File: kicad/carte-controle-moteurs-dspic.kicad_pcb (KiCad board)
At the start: 4 copper layers, 137.2 x 81.3 mm, 73 parts, among them J1 PDB, J10 PWR_IN, J11 GND, J12 5V, J13 3.3V, J14 EN, J15 MOTEUR 1, J16 MOTEUR 2, J17 L1, J18 H1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

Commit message: Optimisation de l'emplacement des composants et de la sérigraphie
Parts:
- ?: renamed from REF**; value Heatsink_Stonecold_HS-132_32x14mm_2xFixation1.5mm -> (none)
- moved R1 16.5 mm to (62.2, 77.5)
- moved R2 13.3 mm to (59.1, 59.7)
- moved U1 10.8 mm to (54.0, 77.5)
- moved ? 10.8 mm to (39.4, 68.6)
- moved J3 9.53 mm to (102.2, 43.2)
- moved C4 8.91 mm to (61.0, 66.7)
- moved C5 8.91 mm to (69.8, 69.2)
- moved RR1 6.38 mm to (129.5, 52.7)
- moved R10 5.08 mm to (129.5, 102.9)
- moved R11 5.08 mm to (124.5, 102.9)
- moved R5 5.08 mm to (108.0, 102.9)
- moved R6 5.08 mm to (105.4, 102.9)
- moved R7 5.08 mm to (100.3, 102.9)
- moved R8 5.08 mm to (132.1, 102.9)
- moved J16 2.84 mm to (118.1, 102.9)
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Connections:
- J10 pad 4: Net-(J10-Pad4) -> (no net)
- J3 pad 1: Net-(J3-Pad1) -> (no net)
- J3 pad 3: Net-(J3-Pad3) -> (no net)
- J6 pad 1: Net-(J6-Pad1) -> (no net)
- J7 pad 1: Net-(J7-Pad1) -> (no net)
- J8 pad 1: Net-(J8-Pad1) -> (no net)
- J9 pad 1: Net-(J9-Pad1) -> (no net)
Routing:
- net Net-(D10-Pad1): track 150.6 -> 137.0 mm
- net /ENABLE: track 91.1 -> 78.0 mm
- net /ALIM_PILES: track 122.5 -> 110.2 mm
- net /QEI1_CHA: track 89.1 -> 77.7 mm
- net /PWM1_H2: track 81.1 -> 70.2 mm
- net /DEBUG_TX: track 40.0 -> 29.3 mm
- net /DEBUG_RX: track 40.8 -> 30.1 mm
- net Net-(D11-Pad1): track 118.5 -> 127.6 mm
- net /PDB: track 58.6 -> 51.3 mm
- net /PWM1_L2: track 83.2 -> 76.2 mm
- net /QEI2_CHA: track 76.6 -> 70.2 mm
- net /QEI1_INDEX: track 88.2 -> 82.1 mm
- net Net-(R1-Pad1): track 2.54 -> 8.25 mm
- net /Mclr: track 58.3 -> 52.8 mm
- net /I2C_DATA: track 98.9 -> 104.2 mm
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
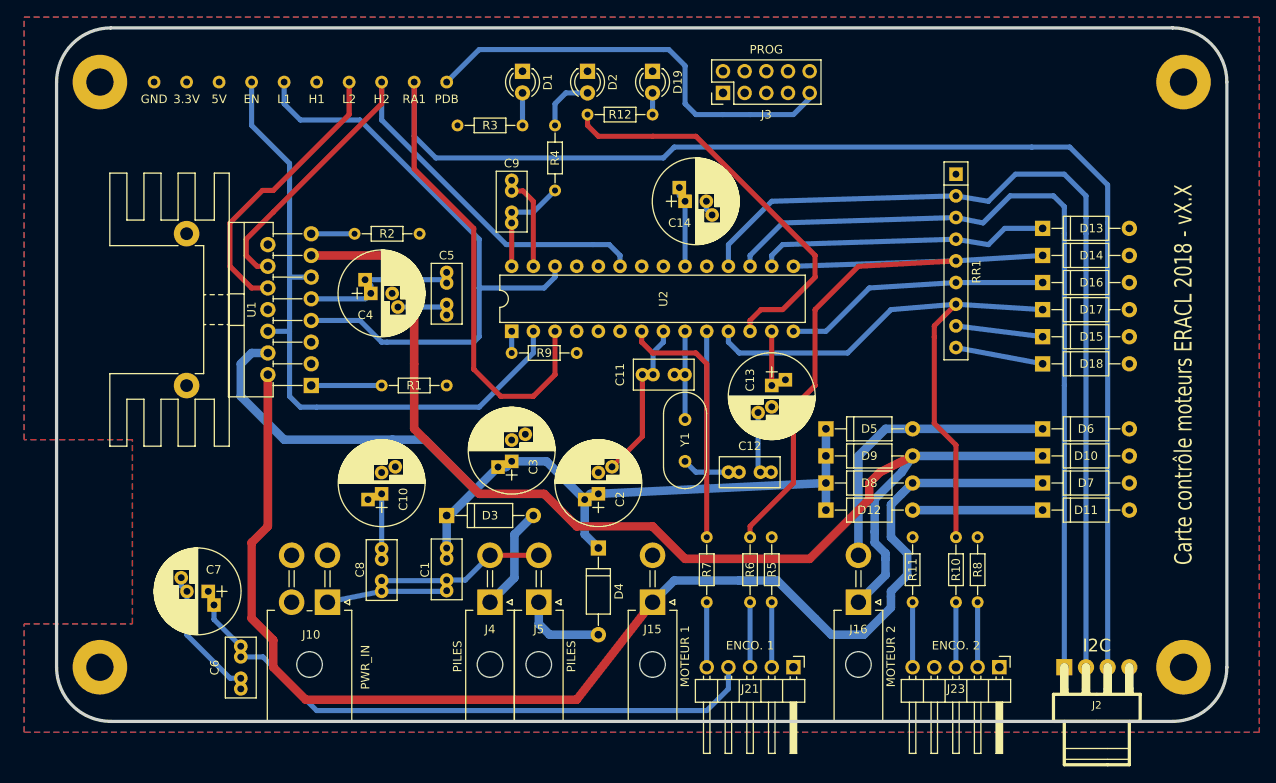
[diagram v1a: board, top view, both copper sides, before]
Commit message: Optimisation du tracé des pistes et des plans et validation typon
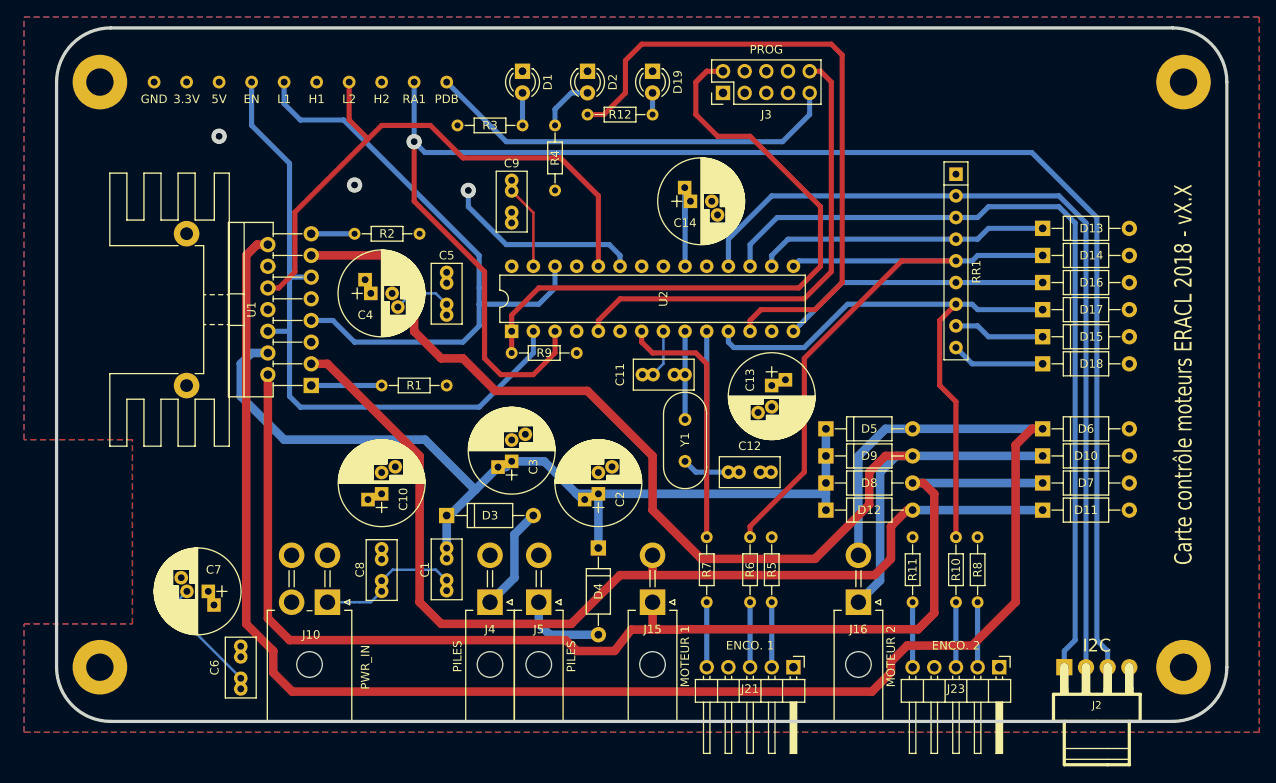
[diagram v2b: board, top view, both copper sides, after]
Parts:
- moved C14 0.63 mm to (98.4, 55.9)
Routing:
- net +5V: track 69.5 -> 201.5 mm, vias 0 -> 1
- net Net-(D5-Pad2): track 137.7 -> 203.2 mm
- net GND: track 98.8 -> 61.2 mm
- net Net-(R12-Pad2): track 47.8 -> 76.6 mm
- net /Mclr: track 52.8 -> 78.4 mm
- net +3V3: track 46.9 -> 28.1 mm
- net /RA1: track 201.1 -> 185.4 mm, vias 0 -> 1
- net Net-(D11-Pad1): track 127.6 -> 118.7 mm
- net Net-(D7-Pad1): track 153.2 -> 145.8 mm
- net /PWM1_L2: track 76.2 -> 70.0 mm
- net /QEI2_CHB: track 81.8 -> 76.9 mm
- net /PWM1_H1: track 70.9 -> 75.7 mm, vias 0 -> 1
- net /PWM1_H2: track 70.2 -> 66.5 mm, vias 0 -> 1
- net /I2C_DATA: track 104.2 -> 100.6 mm
- net /PDT: track 68.1 -> 64.8 mm
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- added copper zone on Interne3, net +3V3
- removed copper zone on Interne2, net +3V3
- removed copper zone on Interne3, net +5V
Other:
- net class planes added: clearance 0.254, trace_width 0.3, via_dia 1.80086, via_drill 0.8001

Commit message: Mise à jour de la version dans les cartouches et la sérigraphie
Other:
- board text added: "Carte contrôle moteurs ERACL 2018 - v1.0"
- board text removed: "Carte contrôle moteurs ERACL 2018 - vX.X"
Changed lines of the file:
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@@
     (links 170)
     (no_connects 0)
-    (area 23.939499 35.369499 161.480501 117.030501)
+    (area 20.32 34.29 165.100001 122.364501)
     (thickness 1.6002)
     (drawings 9)
@@
   (title_block
     (title "Carte contrôle moteurs 2A - 2018")
+    (date 2018-02-16)
+    (rev v1.0)
     (company "Centrale Lyon")
     (comment 2 "Contacter G. CHARREAUX (chxguillaume@gmail.com)")
   )
   (layers
-    (0 Dessus signal hide)
+    (0 Dessus signal)
     (1 Interne3 signal)
-    (2 Interne2 signal hide)
-    (31 Dessous signal hide)
+    (2 Interne2 signal)
+    (31 Dessous signal)
     (32 B.Adhes user hide)
     (33 F.Adhes user hide)
@@
     )
   )
-  (gr_text "Carte contrôle moteurs ERACL 2018 - vX.X" (at 156.21 76.2 90) (layer F.SilkS)
+  (gr_text "Carte contrôle moteurs ERACL 2018 - v1.0" (at 156.21 76.2 90) (layer F.SilkS)
     (effects (font (size 2.032 1.524) (thickness 0.3048)))
   )
